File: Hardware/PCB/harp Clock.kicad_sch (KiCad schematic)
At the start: 18 parts, among them J2 PJ-316A-6A, J3 PJ-316A-6A, Q1 AO3401A, U1 74LVC1G157, U3 ADUM1201BRZ

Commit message: OEPSPN & MPN corrected
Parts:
- J2, J3: MPN LCSC Electronics PJ-316A-6A -> PJ-316A-6A
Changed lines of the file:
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@@
 			)
 		)
-		(property "MPN" "LCSC Electronics PJ-316A-6A"
+		(property "MPN" "PJ-316A-6A"
 			(at 44.45 109.22 0)
 			(effects
@@
 			)
 		)
-		(property "MPN" "LCSC Electronics PJ-316A-6A"
-			(at 246.38 109.22 0)
-			(effects
+		(property "MPN" "PJ-316A-6A"
+			(at 246.38 109.22 0)
+			(effects

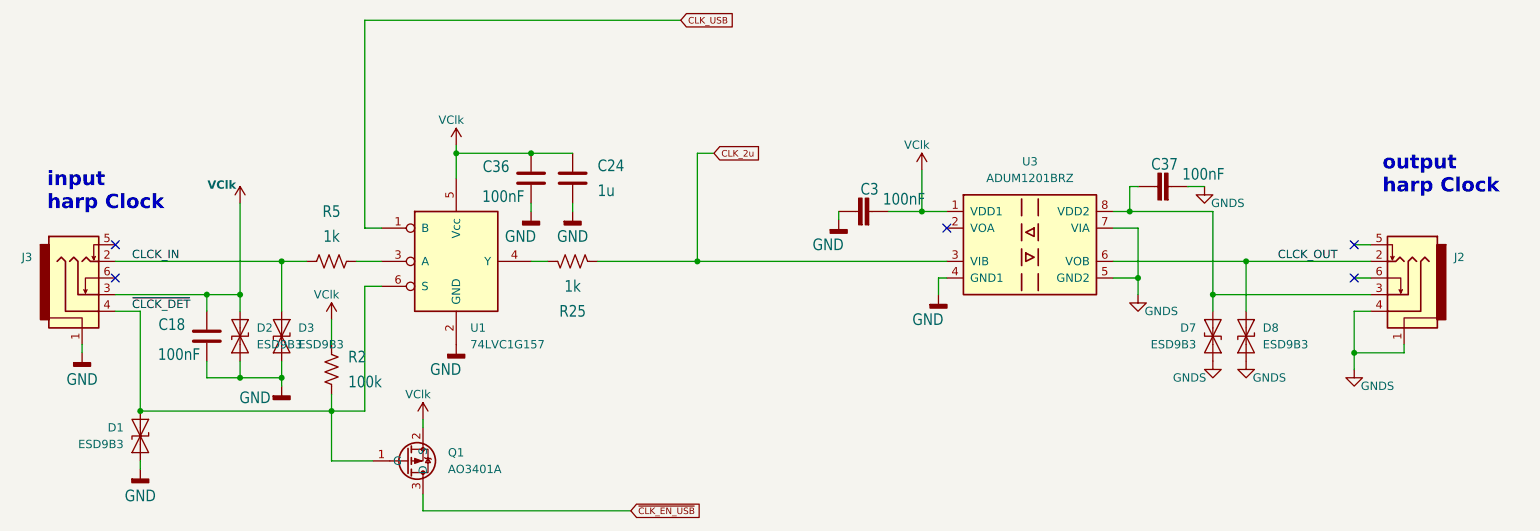
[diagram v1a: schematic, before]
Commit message: 1º commit com v.1.1 corrigida
	. fich USB-C; pinos B10 & B11 trocados
	. Rs de PDown nos rails USB CC1 & CC2
	. rail de VClck deixa de existir: VClck = +3V3
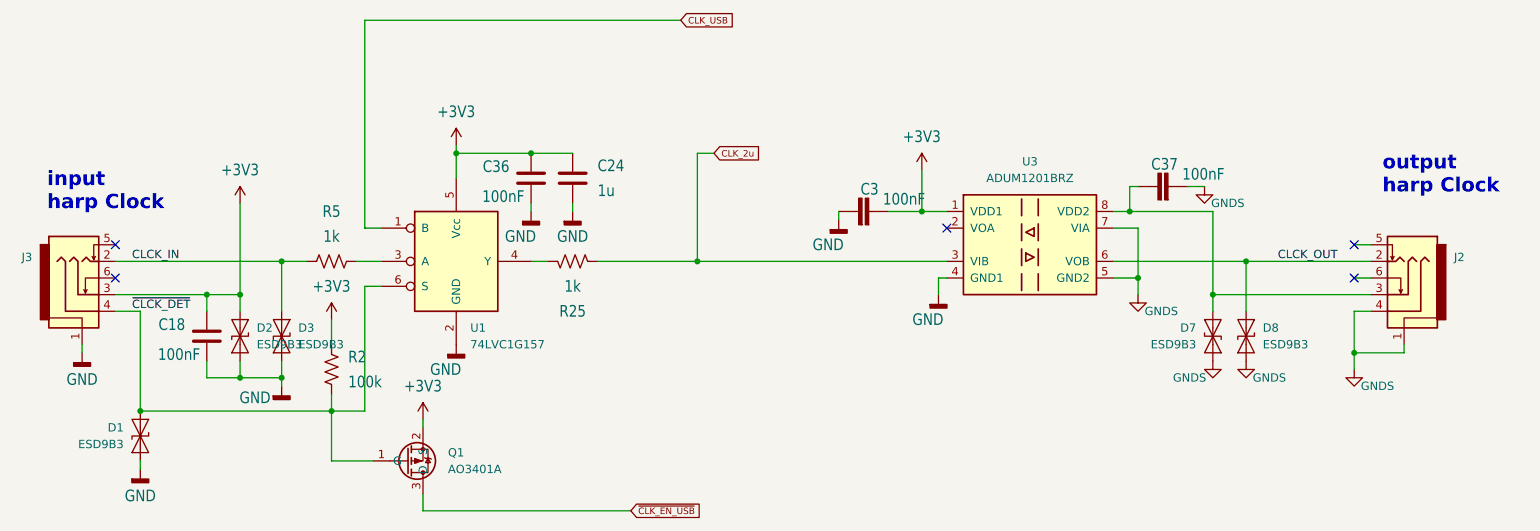
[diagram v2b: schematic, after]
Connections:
- net VClk renamed +3V3
